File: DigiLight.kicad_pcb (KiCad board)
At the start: 2 copper layers, 95 x 70 mm, 88 parts, among them IC1 MAX9814 Module, J1 IN_1, J2 IN_2, J3 POWER (5V/3A), J4 APU-2, J5 112J-TDAR-R-Micro_SD_Card, J6 WS2811, Q1 BC846, Q2 BC846, Q3 IRLML6402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

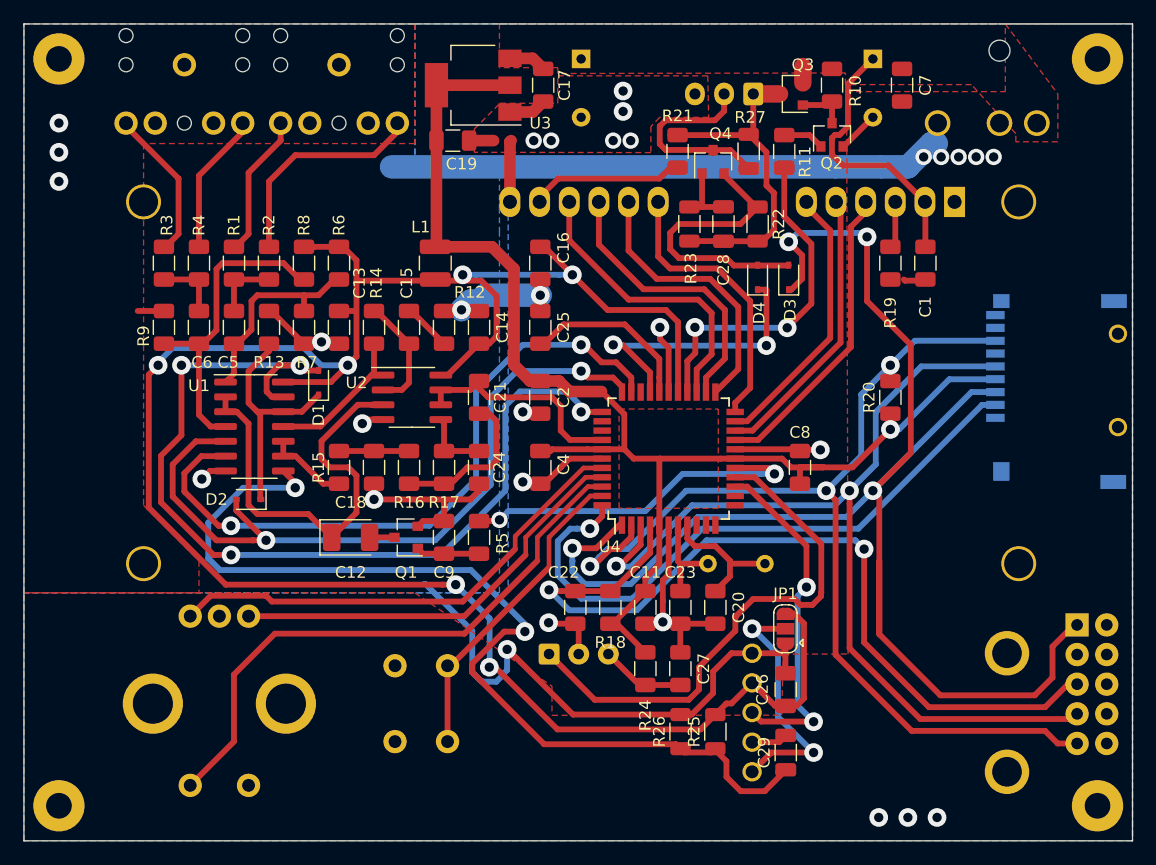
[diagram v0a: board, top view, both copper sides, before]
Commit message: Migrating to Kicad 6.0. Removed external links.
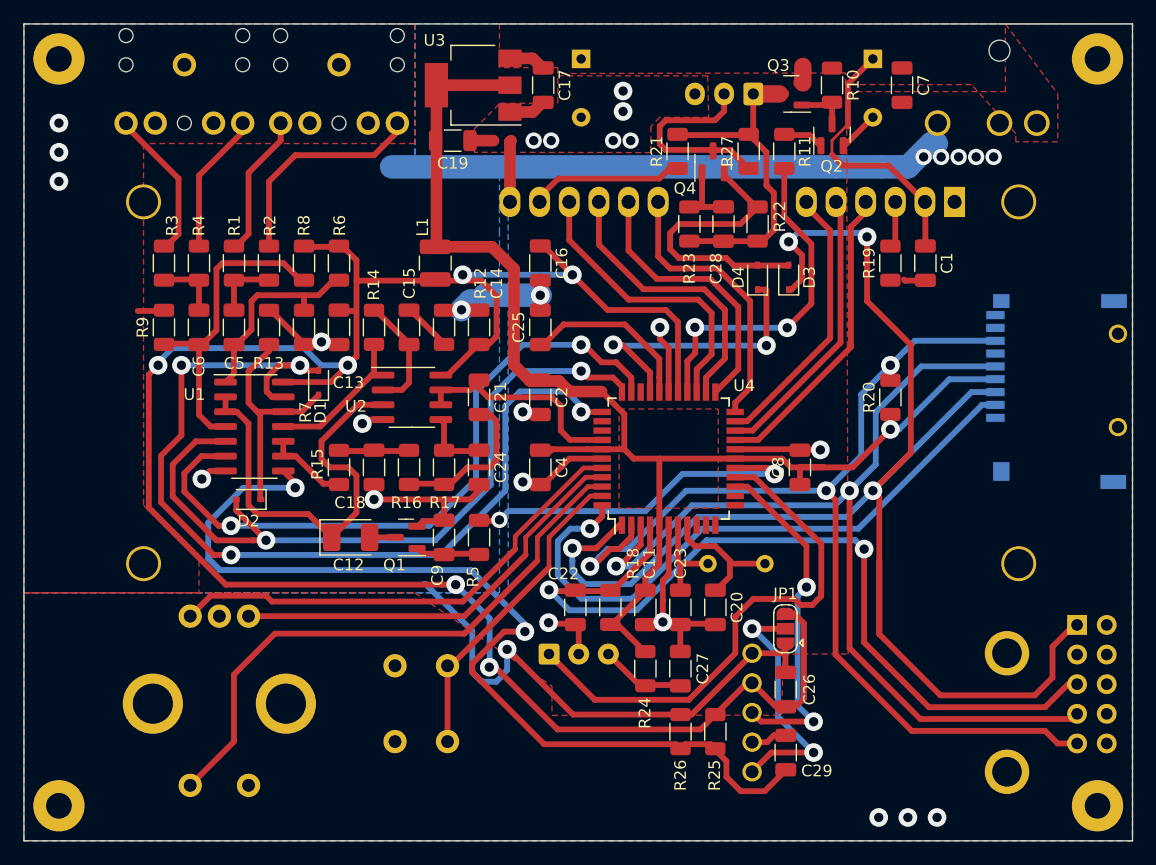
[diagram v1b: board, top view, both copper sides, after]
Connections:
- J3 pad 3: Net-(J3-Pad3) -> unconnected-(J3-Pad3)
- J4 pad 2: Net-(J4-Pad2) -> unconnected-(J4-Pad2)
- J4 pad 3: Net-(J4-Pad3) -> unconnected-(J4-Pad3)
- J5 pad 1: Net-(J5-Pad1) -> unconnected-(J5-Pad1)
- J5 pad 8: Net-(J5-Pad8) -> unconnected-(J5-Pad8)
- J5 pad 9: Net-(J5-Pad9) -> unconnected-(J5-Pad9)
- U4 pad 10: Net-(U4-Pad10) -> unconnected-(U4-Pad10)
- U4 pad 11: Net-(U4-Pad11) -> unconnected-(U4-Pad11)
- U4 pad 12: Net-(U4-Pad12) -> unconnected-(U4-Pad12)
- U4 pad 13: Net-(U4-Pad13) -> unconnected-(U4-Pad13)
- U4 pad 31: Net-(U4-Pad31) -> unconnected-(U4-Pad31)
- U4 pad 35: Net-(U4-Pad35) -> unconnected-(U4-Pad35)
- U4 pad 36: Net-(U4-Pad36) -> unconnected-(U4-Pad36)
- U4 pad 9: Net-(U4-Pad9) -> unconnected-(U4-Pad9)
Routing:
- net GNDA: track 127.4 -> 126.4 mm
- net Net-(C29-Pad1): track 83.2 -> 84.1 mm
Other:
- net class Default removed

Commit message: Maked production version of PCB
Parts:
- moved Q2 1.03 mm to (215.6, 64.3)
- moved J4 0.45 mm to (237.2, 105.9)
- moved C10 0.36 mm to (219.4, 57.0)
- moved Y1 0.14 mm to (210.5, 100.1)
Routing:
- net Net-(C29-Pad1): track 84.1 -> 73.2 mm
- net /MOSI: track 129.3 -> 118.8 mm
- net GND: track 65.7 -> 56.7 mm, vias 20 -> 9
- net GNDA: track 126.4 -> 119.2 mm, vias 10 -> 7
- net VDDA: track 183.2 -> 177.1 mm
- net /MC_GAIN: track 29.8 -> 24.4 mm, vias 2 -> 1
- net Net-(IC1-Pad5): track 21.6 -> 16.6 mm, vias 2 -> 1
- net /SD_CS: track 53.8 -> 49.2 mm
- net /IN_1_SEL: track 81.3 -> 77.4 mm
- net /MISO: track 91.0 -> 87.3 mm
- net /MC_SEL: track 58.7 -> 55.4 mm
- net /IN_2_SEL: track 64.1 -> 61.2 mm
- net Net-(C5-Pad1): track 18.3 -> 17.6 mm
- net Net-(Q2-Pad3): track 4.47 -> 5.06 mm

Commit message: Small cosmetic edits. Production gerber files.
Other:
- rule pad_to_mask_clearance: 0.051 -> 0
- board text added: "DigiLight-M"
